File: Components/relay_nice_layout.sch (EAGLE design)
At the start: 1 part

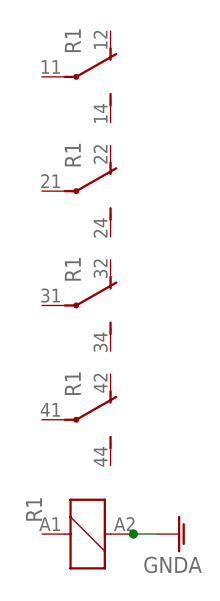
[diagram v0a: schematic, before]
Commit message: Fixing GND terminal on relay
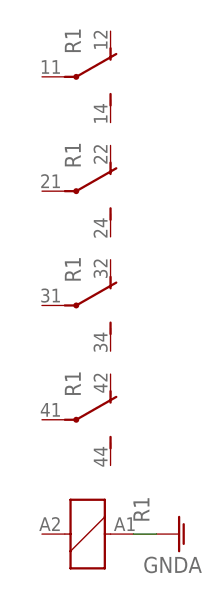
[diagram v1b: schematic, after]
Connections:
- net GNDA: now also R11.1; no longer R11.2
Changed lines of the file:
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@@
 <?xml version="1.0" encoding="utf-8"?>
 <!DOCTYPE eagle SYSTEM "eagle.dtd">
-<eagle version="8.1.0">
+<eagle version="8.2.1">
 <drawing>
 <settings>
@@
 <instances>
 <instance part="GND1" gate="1" x="73.66" y="17.78" rot="R90"/>
-<instance part="R1" gate="1" x="63.5" y="17.78" rot="R90"/>
+<instance part="R1" gate="1" x="63.5" y="17.78" rot="MR90"/>
 <instance part="R1" gate="2" x="60.96" y="68.58" rot="MR90"/>
 <instance part="R1" gate="3" x="60.96" y="55.88" rot="MR90"/>
@@
 <net name="GNDA" class="0">
 <segment>
-<pinref part="R1" gate="1" pin="2"/>
-<junction x="68.58" y="17.78"/>
+<pinref part="R1" gate="1" pin="1"/>
 <pinref part="GND1" gate="1" pin="GNDA"/>
 <wire x1="68.58" y1="17.78" x2="71.12" y2="17.78" width="0.1524" layer="91"/>
